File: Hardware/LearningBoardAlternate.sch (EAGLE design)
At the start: 54 parts, among them IC1 FT230XS-RFT230XS-R

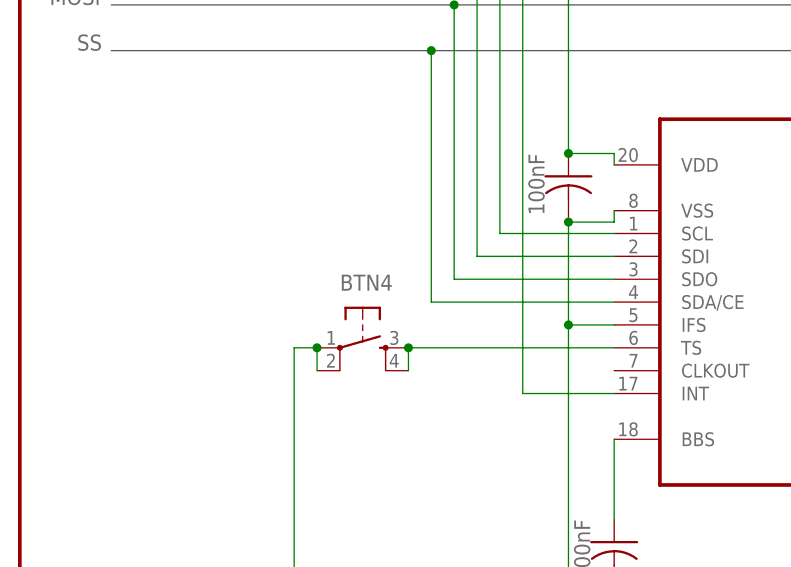
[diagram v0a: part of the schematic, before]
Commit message: Updated parts on board and part labels
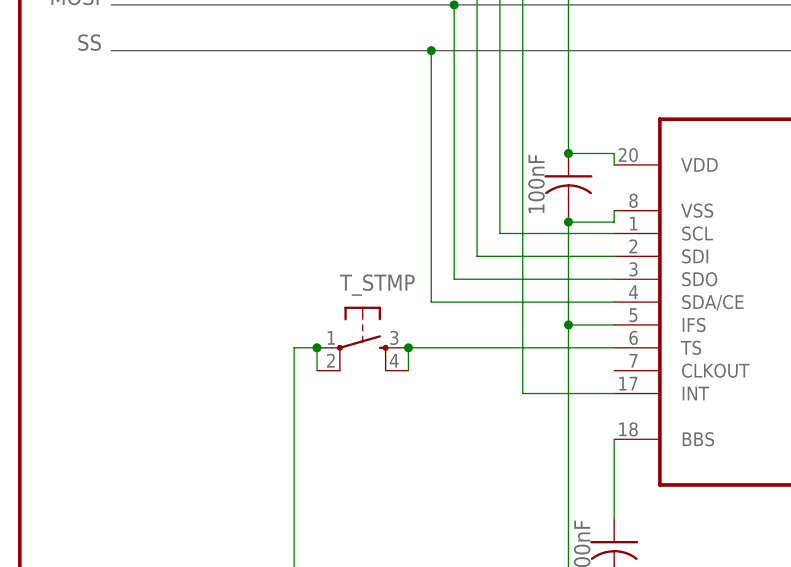
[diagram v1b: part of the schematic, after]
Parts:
- renumbered BTN4 to T_STMP
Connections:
- net BASE renamed DIN
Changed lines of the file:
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@@
 <part name="RPU16" library="SparkFun-Passives" deviceset="RESISTOR" device="0805-RES" value="4.7k"/>
 <part name="RPU17" library="SparkFun-Passives" deviceset="RESISTOR" device="0805-RES" value="4.7k"/>
-<part name="BTN4" library="SparkFun-Electromechanical" deviceset="TAC_SWITCH" device="PTH"/>
+<part name="T_STMP" library="SparkFun-Electromechanical" deviceset="TAC_SWITCH" device="PTH"/>
 <part name="RPU4" library="SparkFun-Passives" deviceset="RESISTOR" device="0805-RES" value="10k"/>
 <part name="C3" library="resistor" deviceset="C-US" device="C0805" value="100nF"/>
@@
 <attribute name="VALUE" x="15.24" y="4.064" size="1.778" layer="96"/>
 </instance>
-<instance part="BTN4" gate="S" x="38.1" y="195.58"/>
+<instance part="T_STMP" gate="S" x="38.1" y="195.58"/>
 <instance part="RPU4" gate="G$1" x="55.88" y="250.19" smashed="yes" rot="R270">
 <attribute name="VALUE" x="54.356" y="251.206" size="1.778" layer="96" rot="R180"/>
@@
 </segment>
 <segment>
-<pinref part="BTN4" gate="S" pin="1"/>
-<pinref part="BTN4" gate="S" pin="2"/>
+<pinref part="T_STMP" gate="S" pin="1"/>
+<pinref part="T_STMP" gate="S" pin="2"/>
 <wire x1="33.02" y1="195.58" x2="33.02" y2="193.04" width="0.1524" layer="91"/>
 <wire x1="30.48" y1="162.56" x2="30.48" y2="195.58" width="0.1524" layer="91"/>
@@
 </segment>
 </net>
-<net name="BASE" class="0">
+<net name="DIN" class="0">
 <segment>
 <pinref part="TRANSMITTER" gate="A" pin="2"/>
@@
 <net name="N$27" class="0">
 <segment>
-<pinref part="BTN4" gate="S" pin="3"/>
-<pinref part="BTN4" gate="S" pin="4"/>
+<pinref part="T_STMP" gate="S" pin="3"/>
+<pinref part="T_STMP" gate="S" pin="4"/>
 <wire x1="43.18" y1="195.58" x2="43.18" y2="193.04" width="0.1524" layer="91"/>
 <pinref part="U$1" gate="G$1" pin="TS"/>
